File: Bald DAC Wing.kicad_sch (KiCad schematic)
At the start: 48 parts, among them J1 PWR, J2 DAC_A_Out, J3 DAC_B_Out, J4 Data Debug HDR, J5 Z_Out, U1 AD5447, U2 AD8065ARTZ, U3 AD8065ARTZ, U4 74LVC574APWR, U5 74LVC574APWR, U6 74LVC1G04, U7 REF3425

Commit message: first edge cut layer
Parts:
- added TP12, TP13: TestPoint_Harwin, My Libraries:Harwin-S1751-46-Test-Point, symbol My Library:TestPoint_Harwin
- C13, C14: footprint Capacitor_SMD:C_0805_2012Metric_Pad1.18x1.45mm_HandSolder -> Capacitor_SMD:C_0402_1005Metric_Pad0.74x0.62mm_HandSolder
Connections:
- net LCLKH: now also TP12.1
- net LCLKL: now also TP13.1
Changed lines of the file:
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@@
 	)
 	(junction
+		(at 185.42 123.19)
+		(diameter 0)
+		(color 0 0 0 0)
+	)
+	(junction
 		(at 373.38 148.59)
 		(diameter 0)
@@
 	(wire
 		(pts
-			(xy 177.8 123.19) (xy 187.96 123.19)
+			(xy 177.8 123.19) (xy 185.42 123.19)
 		)
 		(stroke
@@
 	(wire
 		(pts
+			(xy 185.42 123.19) (xy 187.96 123.19)
+		)
+		(stroke
+			(width 0)
+			(type default)
+		)
+	)
+	(wire
+		(pts
 			(xy 262.89 121.92) (xy 252.73 121.92)
 		)
@@
 	(symbol
 		(lib_id "My Library:TestPoint_Harwin")
+		(at 219.71 123.19 0)
+		(unit 1)
+		(body_style 1)
+		(exclude_from_sim no)
+		(in_bom yes)
+		(on_board yes)
+		(in_pos_files yes)
+		(dnp no)
+		(fields_autoplaced yes)
+		(property "Reference" "TP12"
+			(at 222.25 119.8879 0)
+			(show_name no)
+			(do_not_autoplace no)
+			(effects
+				(font
+					(size 1.27 1.27)
+				)
+				(justify left)
+			)
+		)
+		(property "Value" "TestPoint_Harwin"
+			(at 219.71 118.11 0)
+			(hide yes)
+			(show_name no)
+			(do_not_autoplace no)
+			(effects
+				(font
+					(size 1.27 1.27)
+				)
+			)
+		)
+		(property "Footprint" "My Libraries:Harwin-S1751-46-Test-Point"
+			(at 224.79 123.19 0)
+			(hide yes)
+			(show_name no)
+			(do_not_autoplace no)
+			(effects
+				(font
+					(size 1.27 1.27)
+				)
+			)
+		)
+		(property "Datasheet" ""
+			(at 224.79 123.19 0)
+			(hide yes)
+			(show_name no)
+			(do_not_autoplace no)
+			(effects
+				(font
+					(size 1.27 1.27)
+				)
+			)
+		)
+		(property "Description" "test point"
+			(at 219.71 123.19 0)
+			(hide yes)
+			(show_name no)
+			(do_not_autoplace no)
+			(effects
+				(font
+					(size 1.27 1.27)
+				)
+			)
+		)
+		(property "LCSC" "C3029083"
+			(at 219.71 123.19 0)
+			(hide yes)
+			(show_name no)
+			(do_not_autoplace no)
+			(effects
+				(font
+					(size 1.27 1.27)
+				)
+			)
+		)
+		(pin "1"
+		)
+		(instances
+			(project "Bald DAC Wing"
+				(path "/9844f4b9-7968-409e-b23a-8854509b3e89"
+					(reference "TP12")
+					(unit 1)
+				)
+			)
+		)
+	)
+	(symbol
+		(lib_id "My Library:TestPoint_Harwin")
 		(at 331.47 59.69 0)
 		(unit 1)
@@
 			)
 		)
-		(property "Footprint" "Capacitor_SMD:C_0805_2012Metric_Pad1.18x1.45mm_HandSolder"
+		(property "Footprint" "Capacitor_SMD:C_0402_1005Metric_Pad0.74x0.62mm_HandSolder"
 			(at 312.1152 173.99 0)
 			(hide yes)
@@
 			)
 		)
-		(property "Footprint" "Capacitor_SMD:C_0805_2012Metric_Pad1.18x1.45mm_HandSolder"
+		(property "Footprint" "Capacitor_SMD:C_0402_1005Metric_Pad0.74x0.62mm_HandSolder"
 			(at 323.5452 173.99 0)
 			(hide yes)
@@
 					(unit 1)
 				)
+			)
+		)
+	)
+	(symbol
+		(lib_id "My Library:TestPoint_Harwin")
+		(at 185.42 123.19 0)
+		(unit 1)
+		(body_style 1)
+		(exclude_from_sim no)
+		(in_bom yes)
+		(on_board yes)
+		(in_pos_files yes)
+		(dnp no)
+		(fields_autoplaced yes)
+		(property "Reference" "TP13"
+			(at 187.96 119.8879 0)
+			(show_name no)
+			(do_not_autoplace no)
+			(effects
+				(font
+					(size 1.27 1.27)
+				)
+				(justify left)
+			)
+		)
+		(property "Value" "TestPoint_Harwin"
+			(at 185.42 118.11 0)
+			(hide yes)
+			(show_name no)
+			(do_not_autoplace no)
+			(effects
+				(font
+					(size 1.27 1.27)
+				)
+			)
+		)
+		(property "Footprint" "My Libraries:Harwin-S1751-46-Test-Point"
+			(at 190.5 123.19 0)
+			(hide yes)
+			(show_name no)
+			(do_not_autoplace no)
+			(effects
+				(font
+					(size 1.27 1.27)
+				)
+			)
+		)
+		(property "Datasheet" ""
+			(at 190.5 123.19 0)
+			(hide yes)
+			(show_name no)
+			(do_not_autoplace no)
+			(effects
+				(font
+					(size 1.27 1.27)
+				)
+			)
+		)
+		(property "Description" "test point"
+			(at 185.42 123.19 0)
+			(hide yes)
+			(show_name no)
+			(do_not_autoplace no)
+			(effects
+				(font
+					(size 1.27 1.27)
+				)
+			)
+		)
+		(property "LCSC" "C3029083"
+			(at 185.42 123.19 0)
+			(hide yes)
+			(show_name no)
+			(do_not_autoplace no)
+			(effects
+				(font
+					(size 1.27 1.27)
+				)
+			)
+		)
+		(pin "1"
+		)
+		(instances
+			(project "Bald DAC Wing"
+				(path "/9844f4b9-7968-409e-b23a-8854509b3e89"
+					(reference "TP13")
+					(unit 1)
+				)

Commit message: 1st rough layout
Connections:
- no-connect marks 14 -> 0
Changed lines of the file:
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@@
 		(color 0 0 0 0)
 	)
-	(no_connect
-		(at 73.66 149.86)
-	)
-	(no_connect
-		(at 73.66 182.88)
-	)
-	(no_connect
-		(at 73.66 139.7)
-	)
-	(no_connect
-		(at 73.66 180.34)
-	)
-	(no_connect
-		(at 91.44 129.54)
-	)
-	(no_connect
-		(at 73.66 147.32)
-	)
-	(no_connect
-		(at 73.66 154.94)
-	)
-	(no_connect
-		(at 83.82 129.54)
-	)
-	(no_connect
-		(at 99.06 149.86)
-	)
-	(no_connect
-		(at 73.66 142.24)
-	)
-	(no_connect
-		(at 99.06 139.7)
-	)
-	(no_connect
-		(at 73.66 144.78)
-	)
-	(no_connect
-		(at 73.66 152.4)
-	)
-	(no_connect
-		(at 99.06 147.32)
-	)
 	(wire
 		(pts
@@
 			)
 		)
-		(pin "17"
-		)
-		(pin "18"
-		)
-		(pin "19"
-		)
-		(pin "21"
-		)
 		(pin "10"
 		)
@@
 		(pin "9"
 		)
-		(pin "26"
-		)
 		(pin "16"
 		)
-		(pin "27"
-		)
-		(pin "28"
-		)
 		(pin "5"
 		)
@@
 		(pin "14"
 		)
-		(pin "20"
-		)
-		(pin "22"
-		)
-		(pin "24"
-		)
-		(pin "25"
-		)
-		(pin "23"
-		)
 		(pin "1"

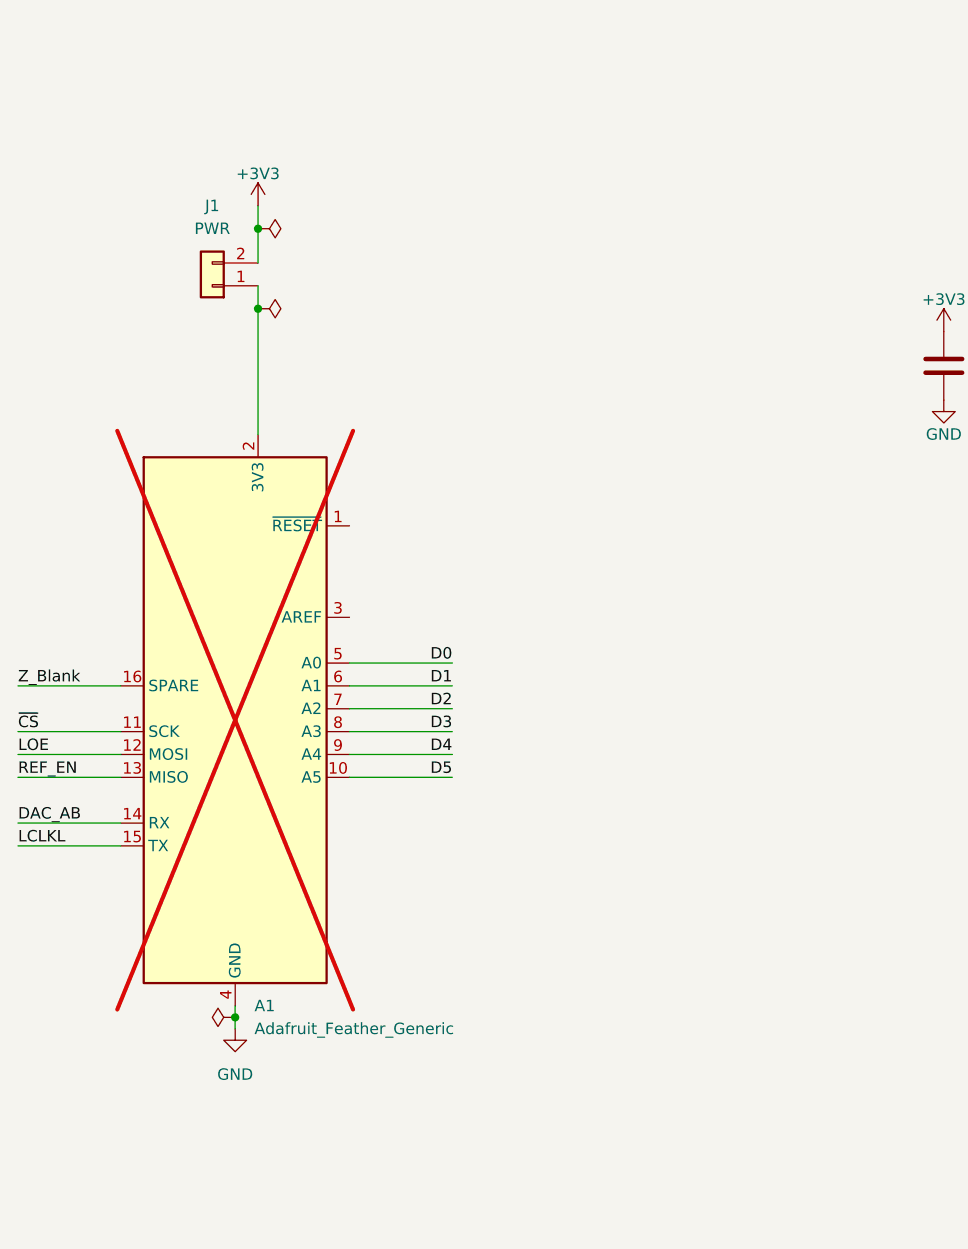
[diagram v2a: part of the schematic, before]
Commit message: ditched feather footprint and went discete. also realized board could be covering
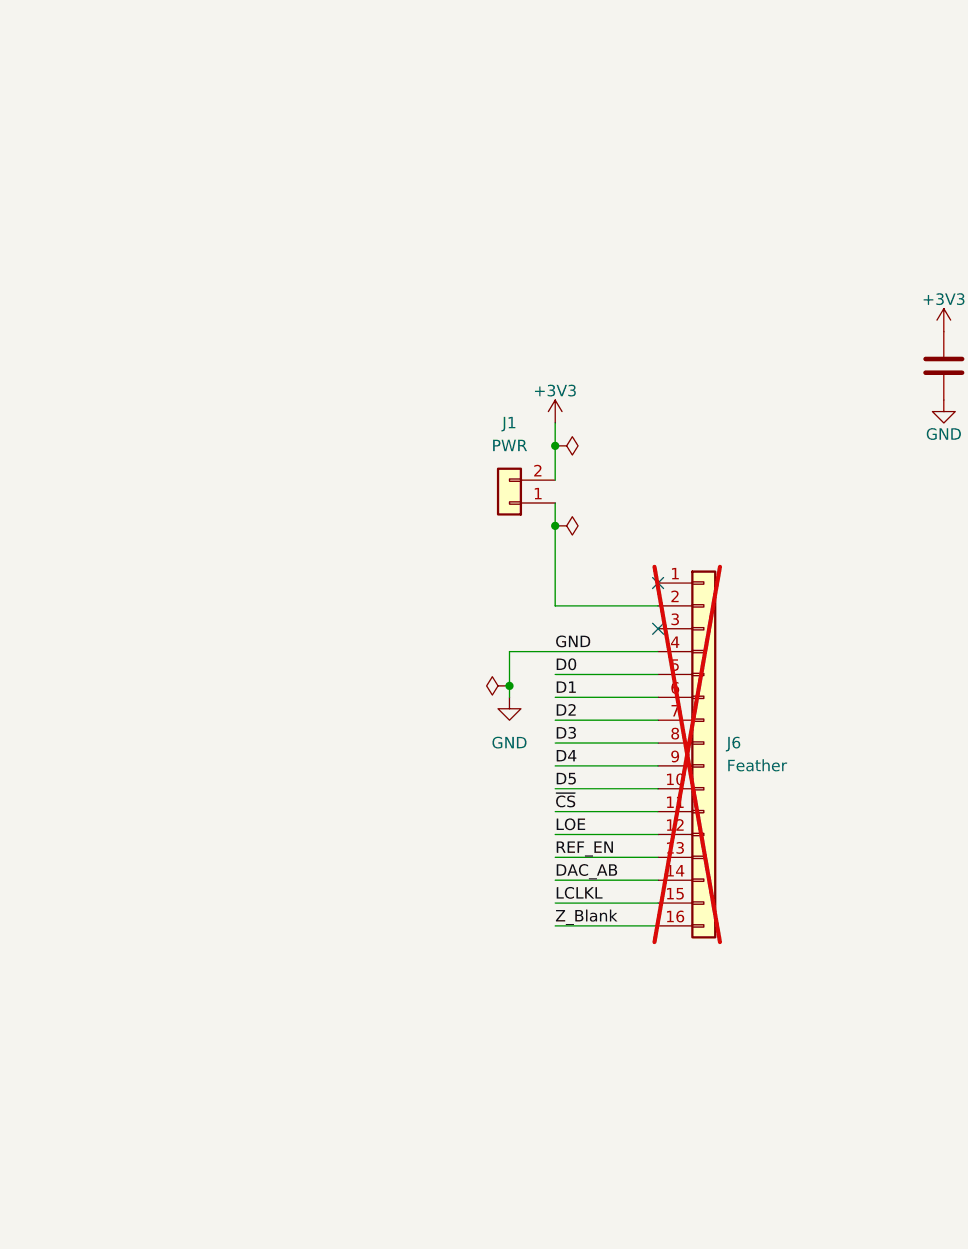
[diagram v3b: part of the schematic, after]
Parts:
- removed A1: Adafruit_Feather_Generic, Module:Adafruit_Feather, symbol MCU_Module:Adafruit_Feather_Generic
- added J6: Feather, Connector_PinSocket_2.54mm:PinSocket_1x16_P2.54mm_Vertical, symbol Connector_Generic:Conn_01x16
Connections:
- net D0: now also J6.5 (Pin_5)
- net D1: now also J6.6 (Pin_6)
- net D2: now also J6.7 (Pin_7)
- net D3: now also J6.8 (Pin_8)
- net D4: now also J6.9 (Pin_9)
- net D5: now also J6.10 (Pin_10)
- net DAC_AB: now also J6.14 (Pin_14)
- net GND: now also J6.4 (Pin_4)
- net LCLKL: now also J6.15 (Pin_15)
- net LOE: now also J6.12 (Pin_12)
- net REF_EN: now also J6.13 (Pin_13)
- net Z_Blank: now also J6.16 (Pin_16)
- net ~{CS}: now also J6.11 (Pin_11)
- net at J1.1 (Pin_1): now also J6.2 (Pin_2)
- no-connect marks 0 -> 2
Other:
- moved on the sheet: J1

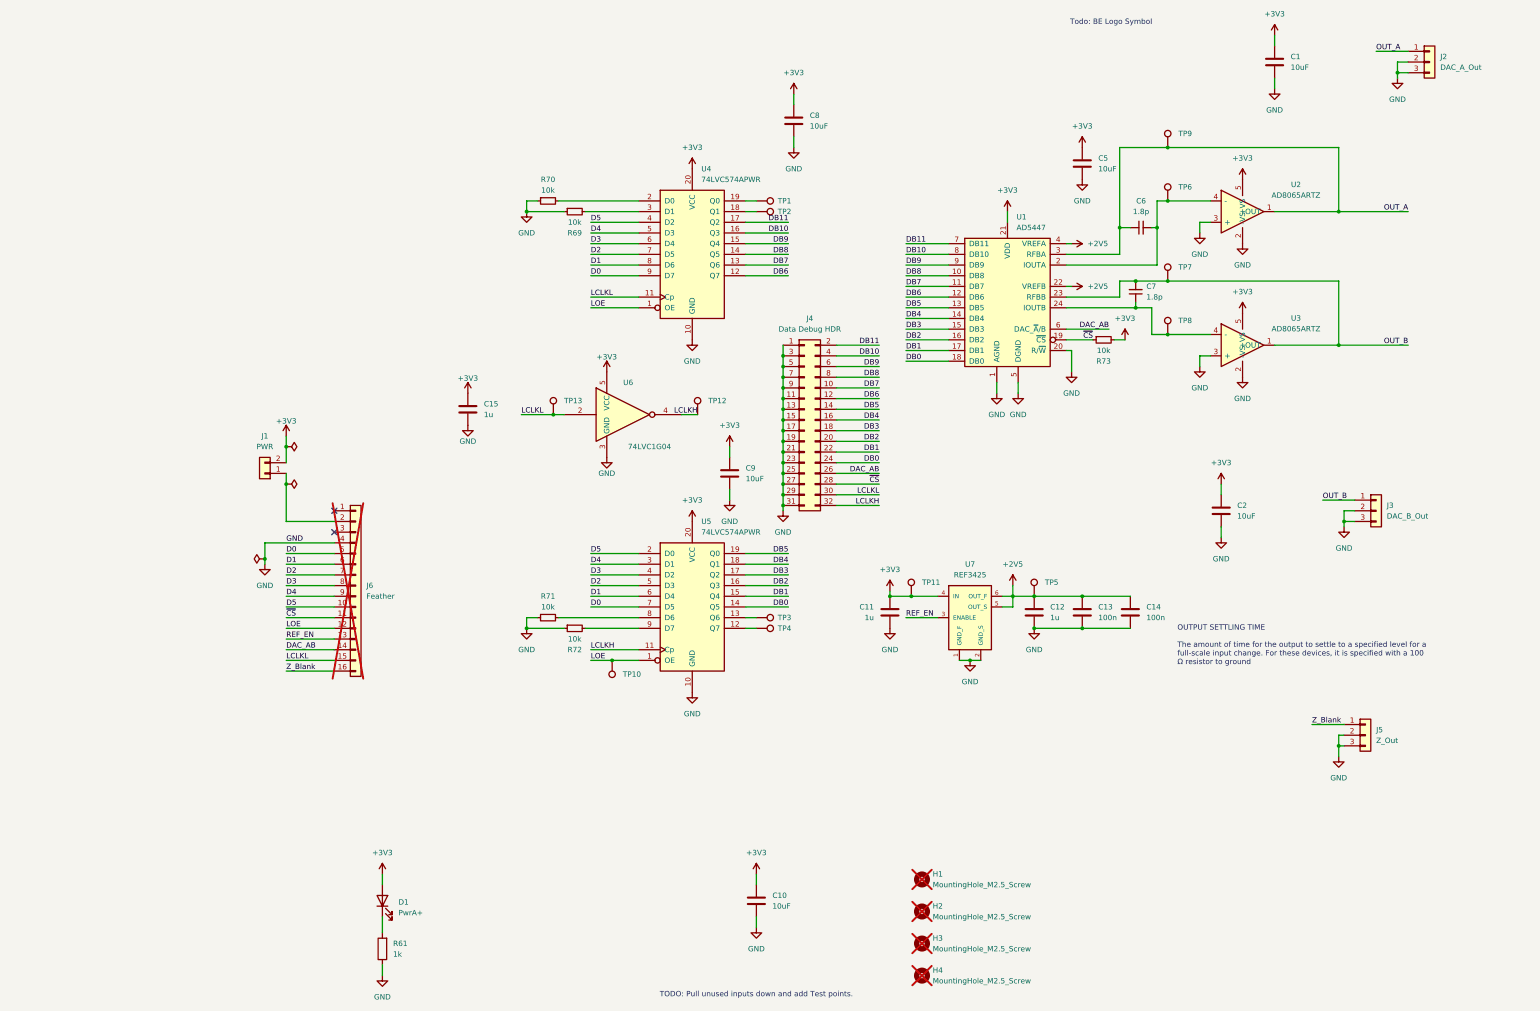
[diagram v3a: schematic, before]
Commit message: broke-up debug headers and squeeshed the board some moar.
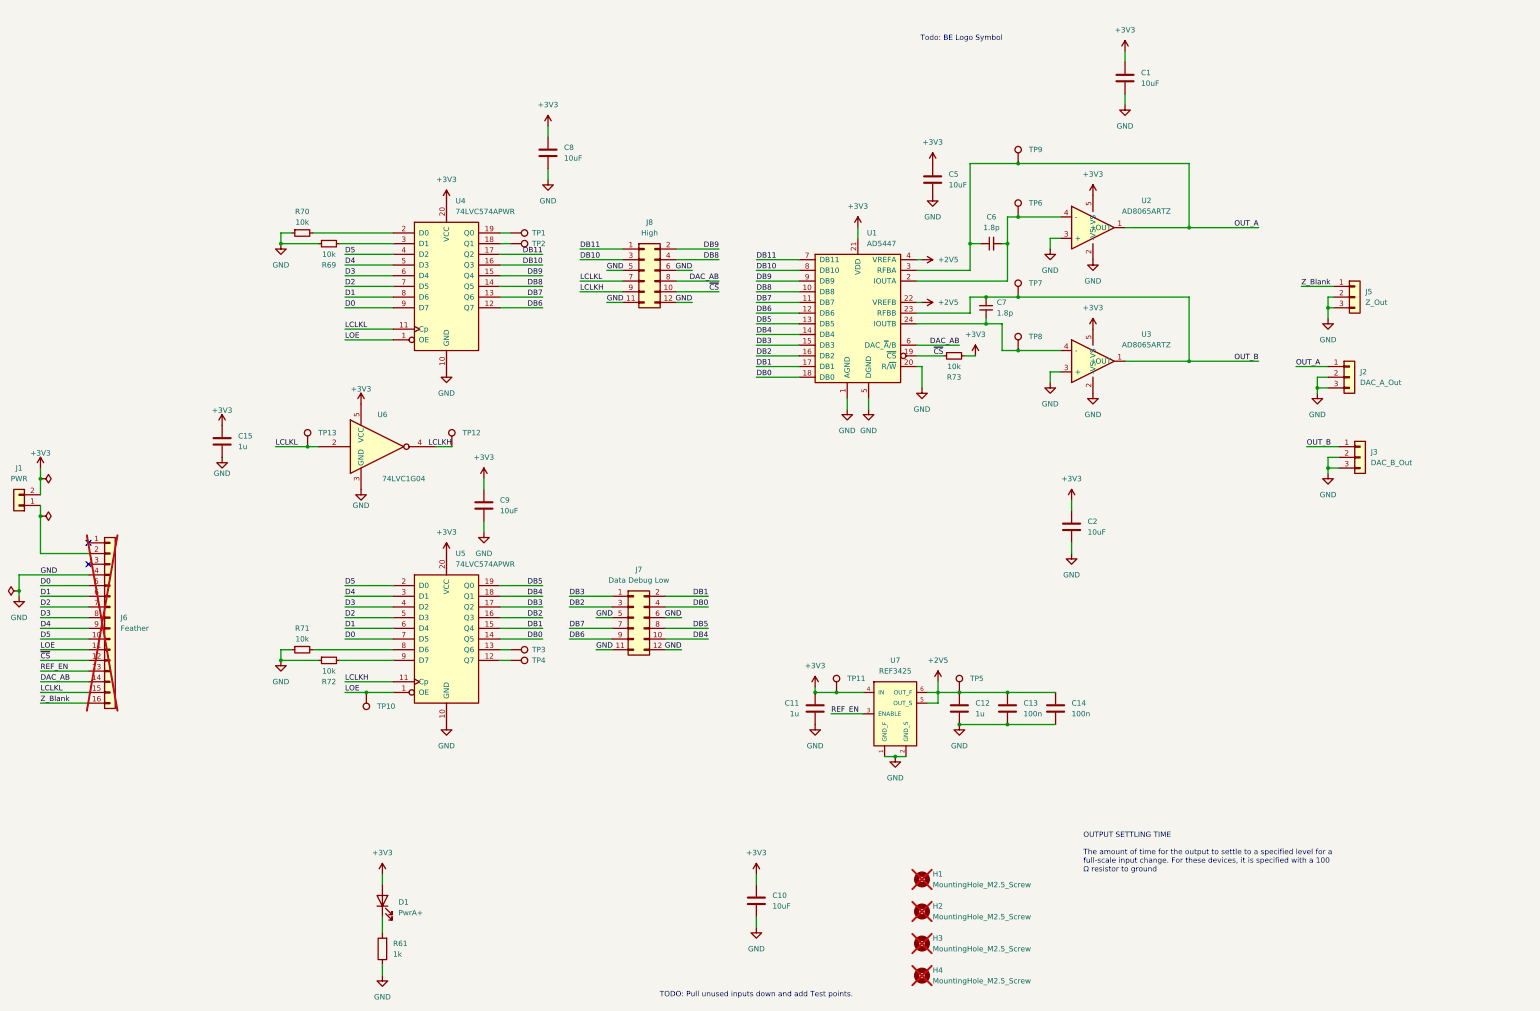
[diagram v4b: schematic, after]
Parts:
- removed J4: Data Debug HDR, Connector_PinHeader_2.00mm:PinHeader_2x16_P2.00mm_Vertical, symbol Connector_Generic:Conn_02x16_Odd_Even
- added J7: Data Debug Low, Connector_PinHeader_2.54mm:PinHeader_2x06_P2.54mm_Vertical, symbol Connector_Generic:Conn_02x06_Odd_Even
- added J8: High, Connector_PinHeader_2.54mm:PinHeader_2x06_P2.54mm_Vertical, symbol Connector_Generic:Conn_02x06_Odd_Even
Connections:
- net DAC_AB: now also J8.8 (Pin_8)
- net DB0: now also J7.4 (Pin_4)
- net DB1: now also J7.2 (Pin_2)
- net DB10: now also J8.3 (Pin_3)
- net DB11: now also J8.1 (Pin_1)
- net DB2: now also J7.3 (Pin_3)
- net DB3: now also J7.1 (Pin_1)
- net DB4: now also J7.10 (Pin_10)
- net DB5: now also J7.8 (Pin_8)
- net DB6: now also J7.9 (Pin_9)
- net DB7: now also J7.7 (Pin_7)
- net DB8: now also J8.4 (Pin_4)
- net DB9: now also J8.2 (Pin_2)
- net GND: now also J7.11 (Pin_11), J7.12 (Pin_12), J7.5 (Pin_5), J7.6 (Pin_6), J8.11 (Pin_11), J8.12 (Pin_12), J8.5 (Pin_5), J8.6 (Pin_6)
- net LCLKH: now also J8.9 (Pin_9)
- net LCLKL: now also J8.7 (Pin_7)
- net LOE: now also J6.11 (Pin_11); no longer J6.12 (Pin_12)
- net ~{CS}: now also J6.12 (Pin_12), J8.10 (Pin_10); no longer J6.11 (Pin_11)
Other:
- moved on the sheet: C1, C11, C12, C13, C14, C15, C2, C5, C6, C7, C8, C9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

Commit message: It's getting there
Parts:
- removed J8: High, Connector_PinHeader_2.54mm:PinHeader_2x06_P2.54mm_Vertical, symbol Connector_Generic:Conn_02x06_Odd_Even
- removed TP12, TP13: TestPoint_Harwin, My Libraries:Harwin-S1751-46-Test-Point, symbol My Library:TestPoint_Harwin
- added J10: Ctrl Debug, Connector_PinHeader_2.54mm:PinHeader_2x04_P2.54mm_Vertical, symbol Connector_Generic:Conn_02x04_Odd_Even
- added J9: Data Debug High, Connector_PinHeader_2.54mm:PinHeader_2x04_P2.54mm_Vertical, symbol Connector_Generic:Conn_02x04_Odd_Even
- J7: footprint Connector_PinHeader_2.54mm:PinHeader_2x06_P2.54mm_Vertical -> Connector_PinHeader_2.54mm:PinHeader_2x04_P2.54mm_Vertical; symbol Connector_Generic:Conn_02x06_Odd_Even -> Connector_Generic:Conn_02x04_Odd_Even
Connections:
- net DAC_AB: now also J10.6 (Pin_6)
- net DB0: now also J7.6 (Pin_6); no longer J7.4 (Pin_4)
- net DB1: now also J7.5 (Pin_5); no longer J7.2 (Pin_2)
- net DB10: now also J9.4 (Pin_4)
- net DB11: now also J9.3 (Pin_3)
- net DB2: now also J7.4 (Pin_4); no longer J7.3 (Pin_3)
- net DB3: now also J7.3 (Pin_3); no longer J7.1 (Pin_1)
- net DB4: now also J7.2 (Pin_2); no longer J7.10 (Pin_10)
- net DB5: now also J7.1 (Pin_1); no longer J7.8 (Pin_8)
- net DB6: now also J9.8 (Pin_8); no longer J7.9 (Pin_9)
- net DB7: now also J9.7 (Pin_7); no longer J7.7 (Pin_7)
- net DB8: now also J9.6 (Pin_6)
- net DB9: now also J9.5 (Pin_5)
- net GND: now also J7.7 (Pin_7), J7.8 (Pin_8), J10.1 (Pin_1), J10.2 (Pin_2), J9.1 (Pin_1), J9.2 (Pin_2); no longer J7.11 (Pin_11), J7.12 (Pin_12), J7.5 (Pin_5), J7.6 (Pin_6)
- net LCLKH: now also J10.7 (Pin_7)
- net LCLKL: now also J10.5 (Pin_5)
- net ~{CS}: now also J10.8 (Pin_8)
- no-connect marks 2 -> 4
